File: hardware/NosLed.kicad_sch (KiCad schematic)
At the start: 7 parts, among them J101 AC, J102 PWM, J103 380OUT, J104 380_BP2876D, J105 LOAD, J107 3V3, J108 380_LNK302PN

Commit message: BP2956XS
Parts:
- added J106: PWM1, TerminalBlock_Phoenix:TerminalBlock_Phoenix_MKDS-1-2-3.81_1x02_P3.81mm_Horizontal, symbol Connector:Screw_Terminal_01x02
- added J109: 380_BP2956XS, TerminalBlock_Phoenix:TerminalBlock_Phoenix_MKDS-1,5-2-5.08_1x02_P5.08mm_Horizontal, symbol Connector:Screw_Terminal_01x02
- added J110: LOAD2, TerminalBlock_Phoenix:TerminalBlock_Phoenix_MKDS-1,5-2-5.08_1x02_P5.08mm_Horizontal, symbol Connector:Screw_Terminal_01x02
- J102: value PWM -> PWM2
- J105: value LOAD -> LOAD2
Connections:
- net ACInput/380V: now also J109.1 (Pin_1)
- net ACInput/GND: now also J106.2 (Pin_2), J109.2 (Pin_2)
- new net BP2956XS/LOAD+: J110.1 (Pin_1)
- new net BP2956XS/LOAD-: J110.2 (Pin_2)
- new net BP2956XS/PWM: J106.1 (Pin_1)
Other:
- sheet BP2956XS ports: added 380V, GND, LOAD+, LOAD-, PWM; removed none
- moved on the sheet: J105

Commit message: Prototype
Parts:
- removed J106: PWM1, TerminalBlock_Phoenix:TerminalBlock_Phoenix_MKDS-1-2-3.81_1x02_P3.81mm_Horizontal, symbol Connector:Screw_Terminal_01x02
- removed J109: 380_BP2956XS, TerminalBlock_Phoenix:TerminalBlock_Phoenix_MKDS-1,5-2-5.08_1x02_P5.08mm_Horizontal, symbol Connector:Screw_Terminal_01x02
- removed J110: LOAD2, TerminalBlock_Phoenix:TerminalBlock_Phoenix_MKDS-1,5-2-5.08_1x02_P5.08mm_Horizontal, symbol Connector:Screw_Terminal_01x02
- added J112: LOAD2, TerminalBlock_Phoenix:TerminalBlock_Phoenix_MKDS-1,5-2-5.08_1x02_P5.08mm_Horizontal, symbol Connector:Screw_Terminal_01x02
- added TP101, TP102, TP103, TP104, TP105, TP106: TestPoint, TestPoint:TestPoint_Pad_4.0x4.0mm, symbol Connector:TestPoint
- renumbered J108 to J102, J102 to J105, J104 to J106, J107 to J108, J105 to J110
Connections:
- net ACInput/GND: now also J112.2 (Pin_2), TP101.1, TP106.1
- net BP2956XS/LOAD+: now also TP103.1
- net BP2956XS/LOAD-: now also TP104.1
- net BP2956XS/PWM: now also TP105.1
- net ACInput/380V renamed ACInput/325V
- net ACInput/325V: now also TP102.1
- new net BP8501CH/3V3: J112.1 (Pin_1)
- no-connect marks 1 -> 2
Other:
- added sheet BP8501CH (BP8501CH.kicad_sch)
- sheet ACInput ports: added 325V; removed 380V
- sheet BP2876D ports: added 325V; removed 380V
- sheet BP2956XS ports: added 325V; removed 380V
- sheet LNK302PN ports: added 325V; removed 380V

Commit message: Tracing draft
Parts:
- removed J102: 380_LNK302PN, TerminalBlock_Phoenix:TerminalBlock_Phoenix_MKDS-1,5-2-5.08_1x02_P5.08mm_Horizontal, symbol Connector:Screw_Terminal_01x02
- removed J103: 380OUT, TerminalBlock_Phoenix:TerminalBlock_Phoenix_MKDS-1,5-2-5.08_1x02_P5.08mm_Horizontal, symbol Connector:Screw_Terminal_01x02
- removed J105: PWM2, TerminalBlock_Phoenix:TerminalBlock_Phoenix_MKDS-1-2-3.81_1x02_P3.81mm_Horizontal, symbol Connector:Screw_Terminal_01x02
- removed J106: 380_BP2876D, TerminalBlock_Phoenix:TerminalBlock_Phoenix_MKDS-1,5-2-5.08_1x02_P5.08mm_Horizontal, symbol Connector:Screw_Terminal_01x02
- removed J108: 3V3, TerminalBlock_Phoenix:TerminalBlock_Phoenix_MKDS-1,5-2-5.08_1x02_P5.08mm_Horizontal, symbol Connector:Screw_Terminal_01x02
- removed J110, J112: LOAD2, TerminalBlock_Phoenix:TerminalBlock_Phoenix_MKDS-1,5-2-5.08_1x02_P5.08mm_Horizontal, symbol Connector:Screw_Terminal_01x02
- removed TP101, TP102, TP103, TP104, TP105, TP106: TestPoint, TestPoint:TestPoint_Pad_4.0x4.0mm, symbol Connector:TestPoint
- added C101: 1uF, Capacitor_SMD:C_0805_2012Metric_Pad1.18x1.45mm_HandSolder, symbol Device:C
- added C102, C104: 100nF, Capacitor_SMD:C_0805_2012Metric_Pad1.18x1.45mm_HandSolder, symbol Device:C
- added C103: 100uF 10V, Capacitor_THT:CP_Radial_D6.3mm_P2.50mm, symbol Device:C_Polarized
- added H101, H102, H103, H104: MountingHole, MountingHole:MountingHole_3.2mm_M3_Pad_Via, symbol Mechanical:MountingHole_Pad
- added J102: USB_C_Receptacle_USB2.0_16P, Connector_USB:USB_C_Receptacle_HRO_TYPE-C-31-M-12, symbol Connector:USB_C_Receptacle_USB2.0_16P
- added J103: LOAD, TerminalBlock_Phoenix:TerminalBlock_Phoenix_MKDS-1,5-3-5.08_1x03_P5.08mm_Horizontal, symbol Connector:Screw_Terminal_01x03
- added R101, R102: 10K, Resistor_SMD:R_0603_1608Metric_Pad0.98x0.95mm_HandSolder, symbol Device:R
- added R103, R104: 5.1K, Resistor_SMD:R_0603_1608Metric_Pad0.98x0.95mm_HandSolder, symbol Device:R
- added R105, R106: 4.7K, Resistor_SMD:R_0603_1608Metric_Pad0.98x0.95mm_HandSolder, symbol Device:R
- added TP_101: BOOT, NosLib:TestPoint_Pad_1.0x1.0mm, symbol Connector:TestPoint
- added TP_102: GND, NosLib:TestPoint_Pad_1.0x1.0mm, symbol Connector:TestPoint
- added TP_103: EN, NosLib:TestPoint_Pad_1.0x1.0mm, symbol Connector:TestPoint
- added U101: AMS1117-3.3, Package_TO_SOT_SMD:SOT-223-3_TabPin2, symbol Regulator_Linear:AMS1117-3.3
- added U102: ESP32-C3-WROOM-02U, RF_Module:ESP32-C3-WROOM-02U, symbol RF_Module:ESP32-C3-WROOM-02U
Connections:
- net BP2876D_COLD/LOAD+: now also J103.2 (Pin_2)
- net BP2876D_COLD/LOAD-: now also J103.1 (Pin_1)
- new net: J102.A5 (CC1), R103.1
- new net: J102.B5 (CC2), R104.1
- new net 3V3: C103.1, C104.2, R102.1, U101.2 (VO), U102.1 (3V3)
- new net 5V: C102.2, J102.A4 (VBUS), J102.A9 (VBUS), J102.B4 (VBUS), J102.B9 (VBUS), U101.3 (VI)
- new net BOOT: R101.1, TP_101.1, U102.8 (IO9)
- new net BP2876D_WARM/LOAD-: J103.3 (Pin_3)
- new net EN: C101.1, R102.2, TP_103.1, U102.2 (EN)
- new net GND: C101.2, C102.1, C103.2, C104.1, H101.1, H102.1, H103.1, H104.1, J102.A1 (GND), J102.A12 (GND), J102.B1 (GND), J102.B12 (GND), J102.S1 (SHIELD), R101.2, R103.2, R104.2, R105.1, R106.1, TP_102.1, U101.1 (GND), U102.19 (GND), U102.9 (GND)
- new net PWM_COLD: R105.2, U102.4 (IO5)
- new net PWM_WARM: R106.2, U102.3 (IO4)
- new net USB_D+: J102.A6 (D+), J102.B6 (D+), U102.14 (IO19)
- new net USB_D-: J102.A7 (D-), J102.B7 (D-), U102.13 (IO18)
- no-connect marks 2 -> 4
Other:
- sheet BP2956XS renamed BP2876D_COLD
- removed sheet BP2876D
- removed sheet BP8501CH
- added sheet BP2876D_WARM (BP2876D.kicad_sch)
- sheet BP2876D_COLD: file BP2956XS.kicad_sch -> BP2876D.kicad_sch
- sheet LNK302PN ports: added none; removed 3V3
- note added: "ESP32 EN, BOOT"
- note added: "HI VOLTAGE"
- note added: "LDO"
- note added: "USB"
- moved on the sheet: J101

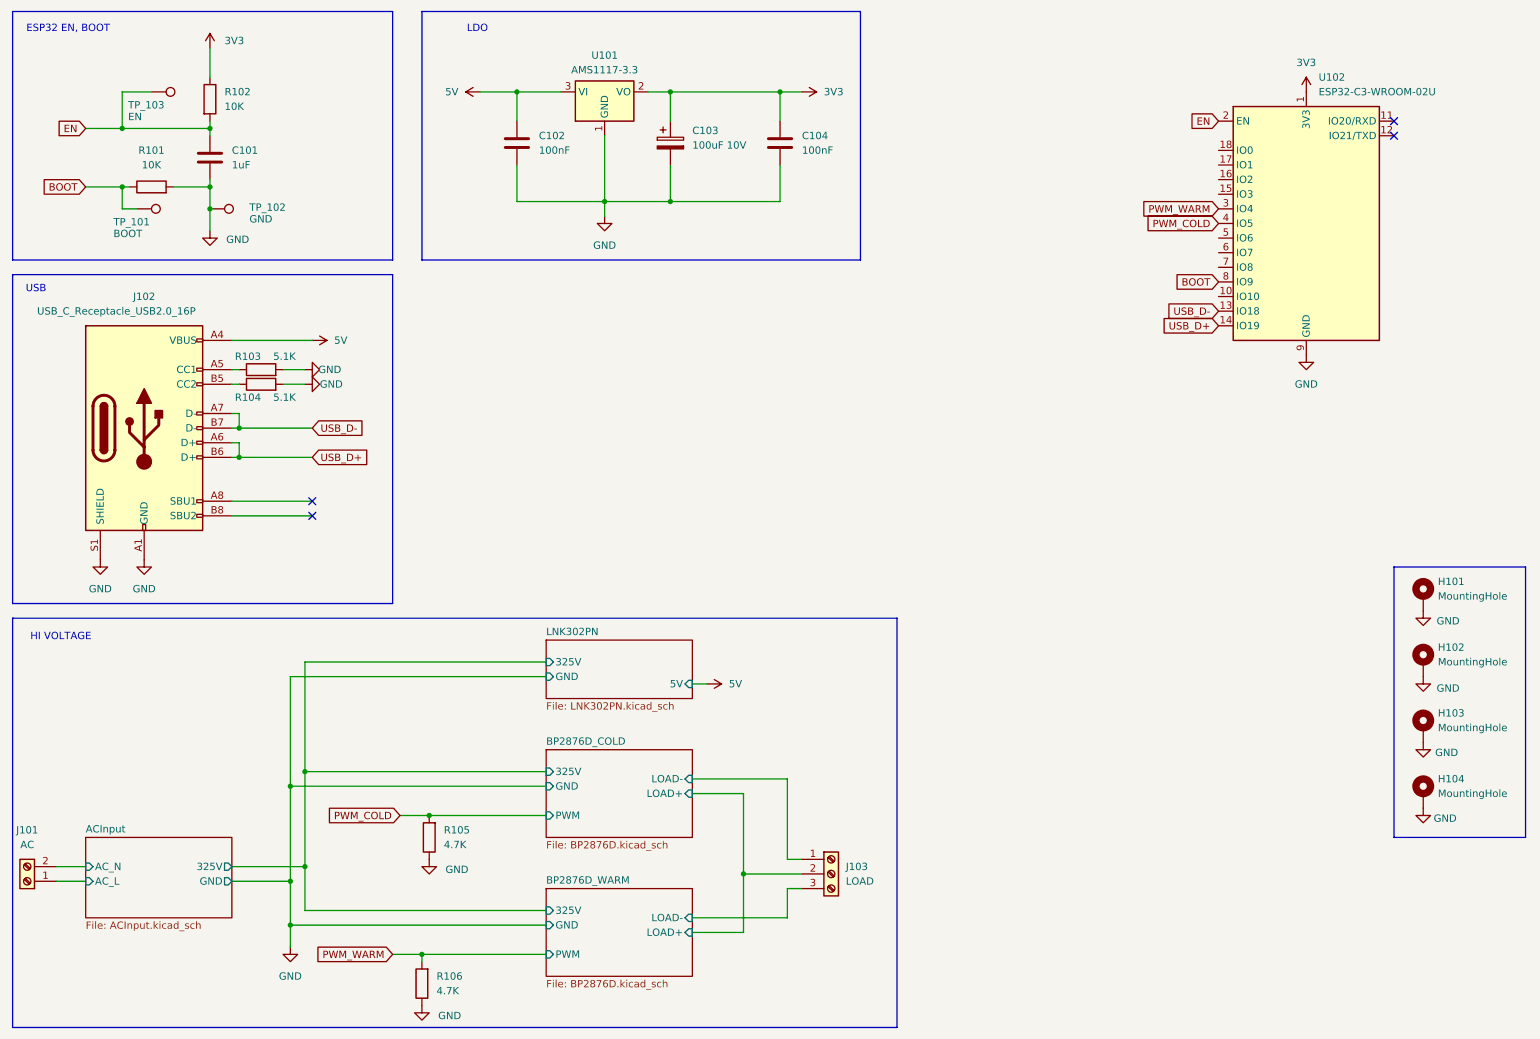
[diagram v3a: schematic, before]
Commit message: Tracing 0.2
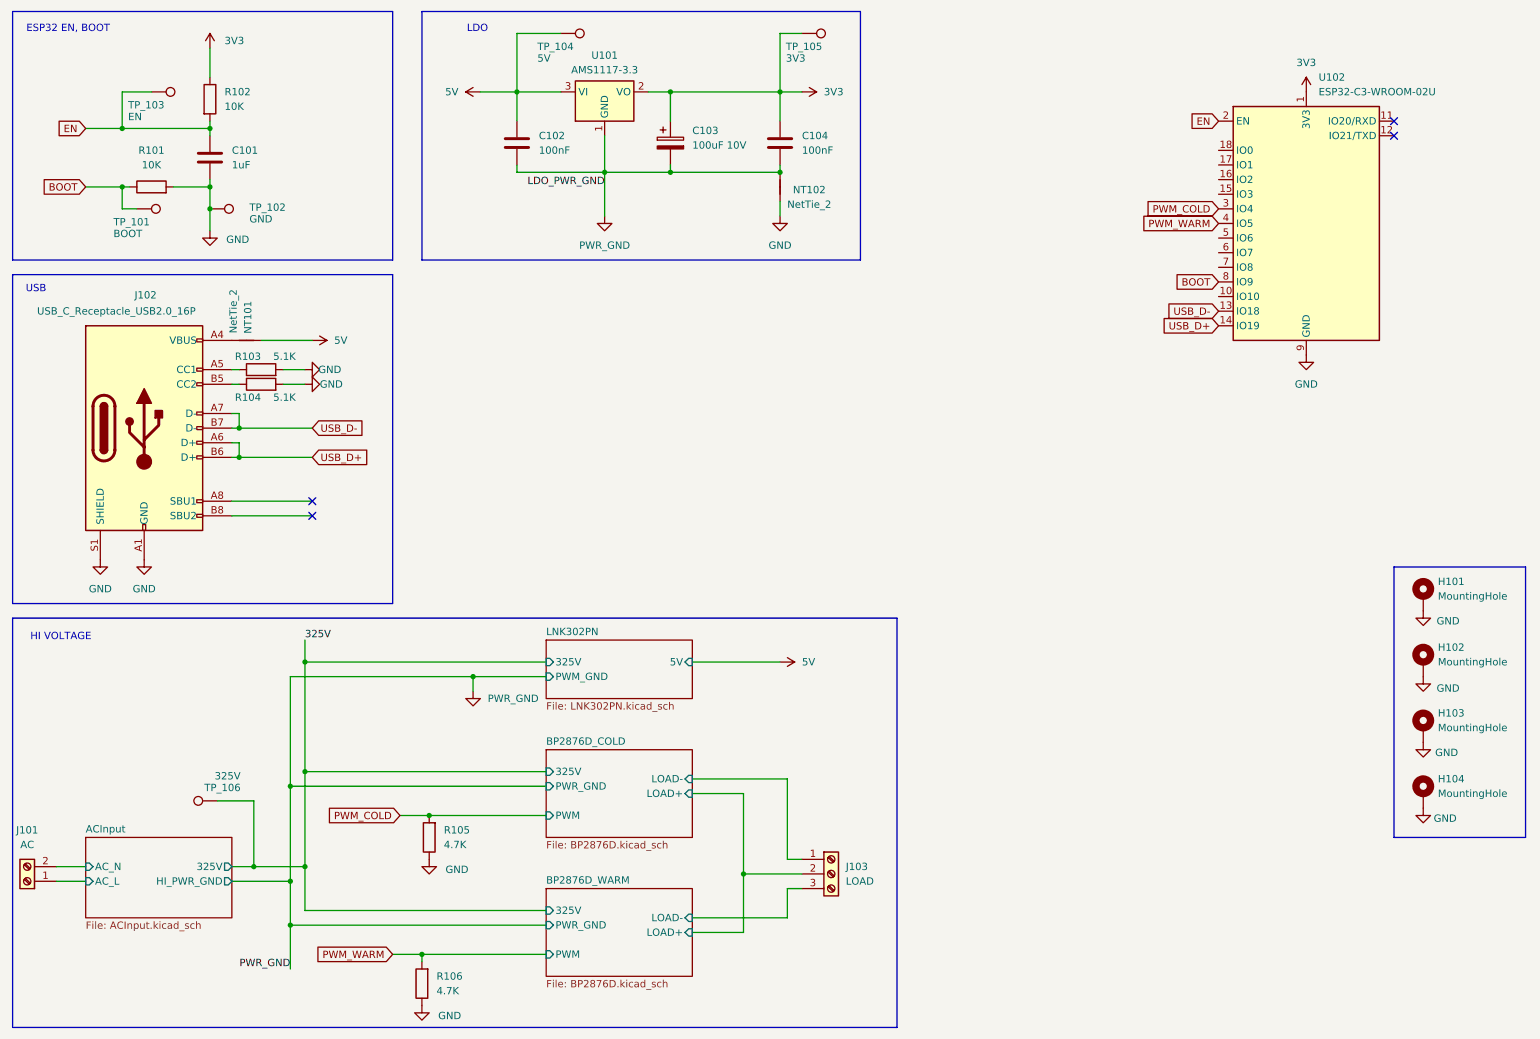
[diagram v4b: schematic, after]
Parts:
- added NT101, NT102: NetTie_2, NetTie:NetTie-2_SMD_Pad0.5mm, symbol Device:NetTie_2
- added TP_104: 5V, NosLib:TestPoint_Pad_1.0x1.0mm, symbol Connector:TestPoint
- added TP_105: 3V3, NosLib:TestPoint_Pad_1.0x1.0mm, symbol Connector:TestPoint
- added TP_106: 325V, NosLib:TestPoint_Pad_1.0x1.0mm, symbol Connector:TestPoint
- C102, C104: footprint Capacitor_SMD:C_0805_2012Metric_Pad1.18x1.45mm_HandSolder -> Capacitor_SMD:C_0603_1608Metric_Pad1.08x0.95mm_HandSolder
- J101: footprint TerminalBlock_Phoenix:TerminalBlock_Phoenix_MKDS-1,5-2-5.08_1x02_P5.08mm_Horizontal -> NosLib:TerminalBlock_Phoenix_MKDS-1,5-2-5.08_1x02_P5.08mm_Horizontal
- J103: footprint TerminalBlock_Phoenix:TerminalBlock_Phoenix_MKDS-1,5-3-5.08_1x03_P5.08mm_Horizontal -> NosLib:TerminalBlock_Phoenix_MKDS-1,5-3-5.08_1x03_P5.08mm_Horizontal
- U102: footprint RF_Module:ESP32-C3-WROOM-02U -> PCM_Espressif:ESP32-C3-WROOM-02U
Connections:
- net 3V3: now also TP_105.1
- net 5V: now also NT101.2, TP_104.1; no longer J102.A4 (VBUS), J102.A9 (VBUS), J102.B4 (VBUS), J102.B9 (VBUS)
- net GND: now also NT102.2; no longer C102.1, C103.2, C104.1, U101.1 (GND)
- net PWM_COLD: now also U102.3 (IO4); no longer U102.4 (IO5)
- net PWM_WARM: now also U102.4 (IO5); no longer U102.3 (IO4)
- new net: J102.A4 (VBUS), J102.A9 (VBUS), J102.B4 (VBUS), J102.B9 (VBUS), NT101.1
- new net 325V: TP_106.1
- new net PWR_GND: C102.1, C103.2, C104.1, NT102.1, U101.1 (GND)
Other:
- sheet ACInput ports: added HI_PWR_GND; removed GND
- sheet BP2876D_COLD ports: added PWR_GND; removed GND
- sheet BP2876D_WARM ports: added PWR_GND; removed GND
- sheet LNK302PN ports: added PWM_GND; removed GND

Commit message: Fixes
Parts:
- renumbered C102 to C101, C103 to C102, C104 to C103, C101 to C104, J102 to J101, J103 to J102, J101 to J103, NT102 to NT101, NT101 to NT102, TP_104 to TP_101, TP_105 to TP_102, TP_101 to TP_103, TP_103 to TP_104, TP_102 to TP_105
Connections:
- net 3V3: now also R101.2
- net GND: no longer R101.2
- no-connect marks 4 -> 12
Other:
- moved on the sheet: C104, R101, R102, TP_103, TP_104, TP_105

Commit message: Use non-hand soldering footprints
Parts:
- C101, C103: footprint Capacitor_SMD:C_0603_1608Metric_Pad1.08x0.95mm_HandSolder -> Capacitor_SMD:C_0603_1608Metric
- C104: footprint Capacitor_SMD:C_0805_2012Metric_Pad1.18x1.45mm_HandSolder -> Capacitor_SMD:C_0805_2012Metric
- R101, R102, R103, R104, R105, R106: footprint Resistor_SMD:R_0603_1608Metric_Pad0.98x0.95mm_HandSolder -> Resistor_SMD:R_0603_1608Metric
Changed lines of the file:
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@@
 			)
 		)
-		(property "Footprint" "Capacitor_SMD:C_0805_2012Metric_Pad1.18x1.45mm_HandSolder"
+		(property "Footprint" "Capacitor_SMD:C_0805_2012Metric"
 			(at 59.3852 49.53 0)
 			(effects
@@
 			)
 		)
-		(property "Footprint" "Resistor_SMD:R_0603_1608Metric_Pad0.98x0.95mm_HandSolder"
+		(property "Footprint" "Resistor_SMD:R_0603_1608Metric"
 			(at 90.678 160.02 90)
 			(effects
@@
 			)
 		)
-		(property "Footprint" "Capacitor_SMD:C_0603_1608Metric_Pad1.08x0.95mm_HandSolder"
+		(property "Footprint" "Capacitor_SMD:C_0603_1608Metric"
 			(at 148.8948 35.56 0)
 			(effects
@@
 			)
 		)
-		(property "Footprint" "Capacitor_SMD:C_0603_1608Metric_Pad1.08x0.95mm_HandSolder"
+		(property "Footprint" "Capacitor_SMD:C_0603_1608Metric"
 			(at 103.1748 35.56 0)
 			(effects
@@
 			)
 		)
-		(property "Footprint" "Resistor_SMD:R_0603_1608Metric_Pad0.98x0.95mm_HandSolder"
+		(property "Footprint" "Resistor_SMD:R_0603_1608Metric"
 			(at 59.69 83.058 90)
 			(effects
@@
 			)
 		)
-		(property "Footprint" "Resistor_SMD:R_0603_1608Metric_Pad0.98x0.95mm_HandSolder"
+		(property "Footprint" "Resistor_SMD:R_0603_1608Metric"
 			(at 48.26 28.448 90)
 			(effects
@@
 			)
 		)
-		(property "Footprint" "Resistor_SMD:R_0603_1608Metric_Pad0.98x0.95mm_HandSolder"
+		(property "Footprint" "Resistor_SMD:R_0603_1608Metric"
 			(at 89.408 185.42 90)
 			(effects
@@
 			)
 		)
-		(property "Footprint" "Resistor_SMD:R_0603_1608Metric_Pad0.98x0.95mm_HandSolder"
+		(property "Footprint" "Resistor_SMD:R_0603_1608Metric"
 			(at 56.642 36.83 90)
 			(effects
@@
 			)
 		)
-		(property "Footprint" "Resistor_SMD:R_0603_1608Metric_Pad0.98x0.95mm_HandSolder"
+		(property "Footprint" "Resistor_SMD:R_0603_1608Metric"
 			(at 59.69 80.518 90)
 			(effects

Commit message: v1.1
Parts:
- C102: value 100uF 10V -> 220uF 25V
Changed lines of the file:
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@@
 			)
 		)
-		(property "Value" "100uF 10V"
+		(property "Value" "220uF 25V"
 			(at 134.62 39.7509 0)
 			(effects

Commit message: Fix holes
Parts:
- H101, H102, H103, H104: footprint MountingHole:MountingHole_3.2mm_M3_Pad_Via -> MountingHole:MountingHole_3.2mm_M3; symbol Mechanical:MountingHole_Pad -> Mechanical:MountingHole
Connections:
- net GND: no longer H101.1, H102.1, H103.1, H104.1
